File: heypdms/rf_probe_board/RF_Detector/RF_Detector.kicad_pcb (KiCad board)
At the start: 2 copper layers, 53 parts, among them J1 Conn_Coaxial, J2 CONN_2x3_Shrouded, U1 LP3985, U2 AD8361, U3 ADS1100

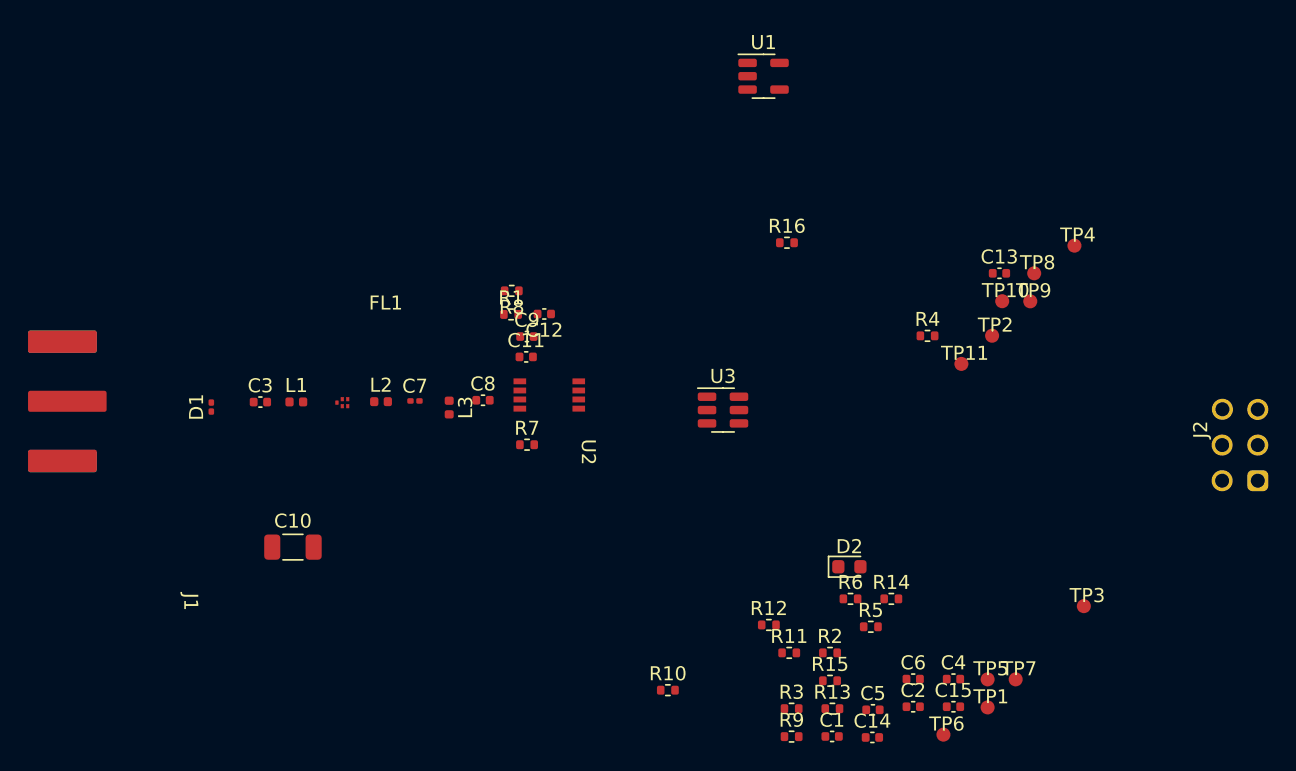
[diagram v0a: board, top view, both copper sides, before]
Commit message: RF_Detector board with zero airwires and most of the silkscreen
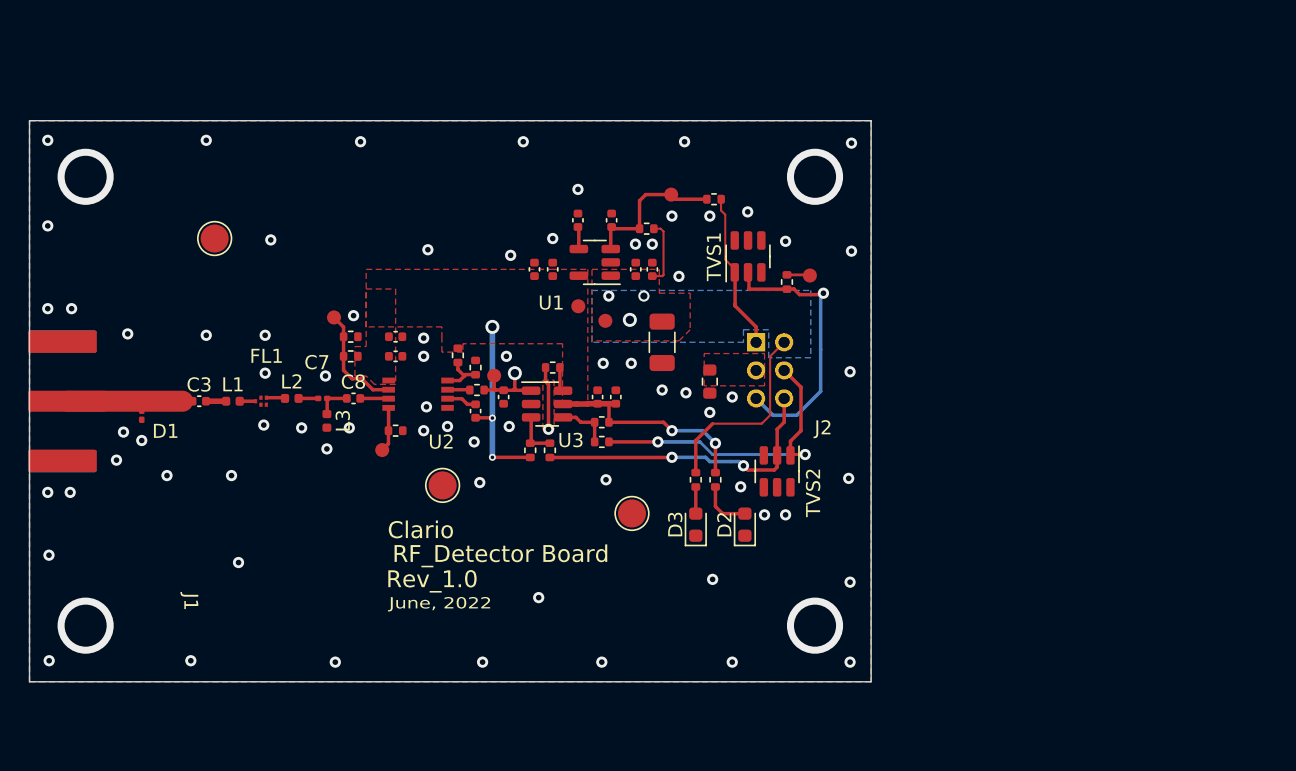
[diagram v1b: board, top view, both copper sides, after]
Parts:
- removed TP1: TestPoint, rf_detector:testpoint_1.0mm
- added C16: 100n, Capacitor_SMD:C_0402_1005Metric, F.Cu at (130.5, 80.1)
- added D3: LED, Diode_SMD:D_0603_1608Metric, F.Cu at (136.5, 101.8)
- added R17: 0, Resistor_SMD:R_0402_1005Metric, F.Cu at (120.9, 92.2)
- added TVS1: TPD2E1B06, Package_TO_SOT_SMD:SOT-23-6, F.Cu at (140.2, 82.7)
- added TVS2: TPD2E1B06, Package_TO_SOT_SMD:SOT-23-6, F.Cu at (142.3, 98.0)
- J2: footprint rf_detector:CONN_2x3_100mil_shrouded_TH_75869-131 -> rf_detector:CONN_2x3_2mm_shrouded_TH
- R12: footprint Resistor_SMD:R_0402_1005Metric -> Resistor_SMD:R_0603_1608Metric
- R13: value 0 -> NP
- R14: value 0 -> 3.3k
- R15: value 10k -> NP
- TP3, TP4, TP5: footprint rf_detector:testpoint_1.0mm -> TestPoint:TestPoint_Pad_D2.0mm
- U3: value ADS1100 -> ADS1100X
- moved TP3 67.4 mm to (102.2, 81.4)
- moved TP7 55.0 mm to (111.0, 86.8)
- moved TP4 48.5 mm to (118.5, 99.0)
- moved TP9 47.4 mm to (114.4, 96.2)
- moved C4 40.9 mm to (126.3, 83.6), turned to -90 degrees
- moved C5 40.7 mm to (128.1, 80.1), turned to -90 degrees
- moved C6 39.8 mm to (125.0, 83.6), turned to -90 degrees
- moved TP8 39.2 mm to (122.4, 90.9)
- moved TP6 38.1 mm to (130.3, 87.0)
- moved C2 36.9 mm to (132.2, 83.6), turned to -90 degrees
- moved C13 36.4 mm to (122.8, 92.7), turned to -90 degrees
- moved C1 35.7 mm to (133.4, 83.6), turned to -90 degrees
- moved R15 34.8 mm to (133.0, 80.7)
- moved R2 34.0 mm to (119.5, 89.7), turned to 90 degrees
- moved J2 33.9 mm to (141.8, 90.8), turned to -90 degrees
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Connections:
- net Net-(C5-Pad2) renamed /LP3985_BYP
- net Net-(J2-Pad1) renamed /CONN_EN
- net Net-(J2-Pad3) renamed /GND_CONN
- net Net-(J2-Pad4) renamed /SDA_CONN
- net Net-(J2-Pad5) renamed /CHK_CONN
- net Net-(J2-Pad6) renamed /SCL_CONN
- net Net-(TP11-Pad1) renamed /CHK
- C1 pad 2: Net-(C1-Pad2) -> /V5D
- C10 pad 2: Net-(C10-Pad2) -> /V5D
- C2 pad 2: Net-(C1-Pad2) -> /V5D
- J2 pad 2: Net-(J2-Pad2) -> /V5D
- R11 pad 1: Net-(TP10-Pad1) -> LP3985_EN
- R14 pad 1: Net-(J2-Pad2) -> /V5D
- R14 pad 2: Net-(C10-Pad2) -> /LED_V5D
- R15 pad 1: Net-(U1-Pad3) -> LP3985_EN
- R15 pad 2: Net-(C1-Pad2) -> /V5D
- TP10 pad 1: Net-(TP10-Pad1) -> LP3985_EN
- TP6 pad 1: Net-(C10-Pad2) -> /V5D
- U1 pad 1: Net-(C1-Pad2) -> /V5D
- U1 pad 3: Net-(U1-Pad3) -> LP3985_EN
- U2 pad 7: /VRMS -> /VRMS_UNFILTERED
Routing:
- net +3V3: track 0.00 -> 28.9 mm, vias 0 -> 5
- net /SDA_CONN: track 0.00 -> 22.3 mm, vias 0 -> 2
- net /SCL_CONN: track 0.00 -> 21.8 mm, vias 0 -> 2
- net /CHK_CONN: track 0.00 -> 19.6 mm, vias 0 -> 1
- net /V5D: track 0.00 -> 18.7 mm, vias 0 -> 3
- net /CONN_EN: track 0.00 -> 11.2 mm
- net LP3985_EN: track 0.00 -> 10.7 mm
- net /RF_IN: track 0.00 -> 8.22 mm
- net /DET_IREF: track 0.00 -> 7.83 mm
- net /VRMS: track 0.00 -> 5.75 mm, vias 0 -> 1
- net GND: track 0.00 -> 4.39 mm, vias 0 -> 77
- net /SDA: track 0.00 -> 4.10 mm
- net /LED_3V3: track 0.00 -> 3.70 mm
- net /SREF: track 0.00 -> 3.33 mm
- net /SCL: track 0.00 -> 3.27 mm
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- added copper zone on F.Cu, net +3V3
- added copper zone on F.Cu, net /GND_CONN
- added copper zone on B.Cu, net /V5D
- added copper zone on F.Cu, net /V5D
- added copper zone on B.Cu, net GND
- added copper zone on F.Cu, net GND
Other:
- board outline added: 60 x 40 mm
- rule pad_to_mask_clearance: 0 -> 0.0508
- board text added: "Clario"
- board text added: "June, 2022"
- board text added: "RF_Detector Board"
- board text added: "Rev_1.0"
